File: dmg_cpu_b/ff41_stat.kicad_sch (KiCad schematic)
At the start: 134 parts

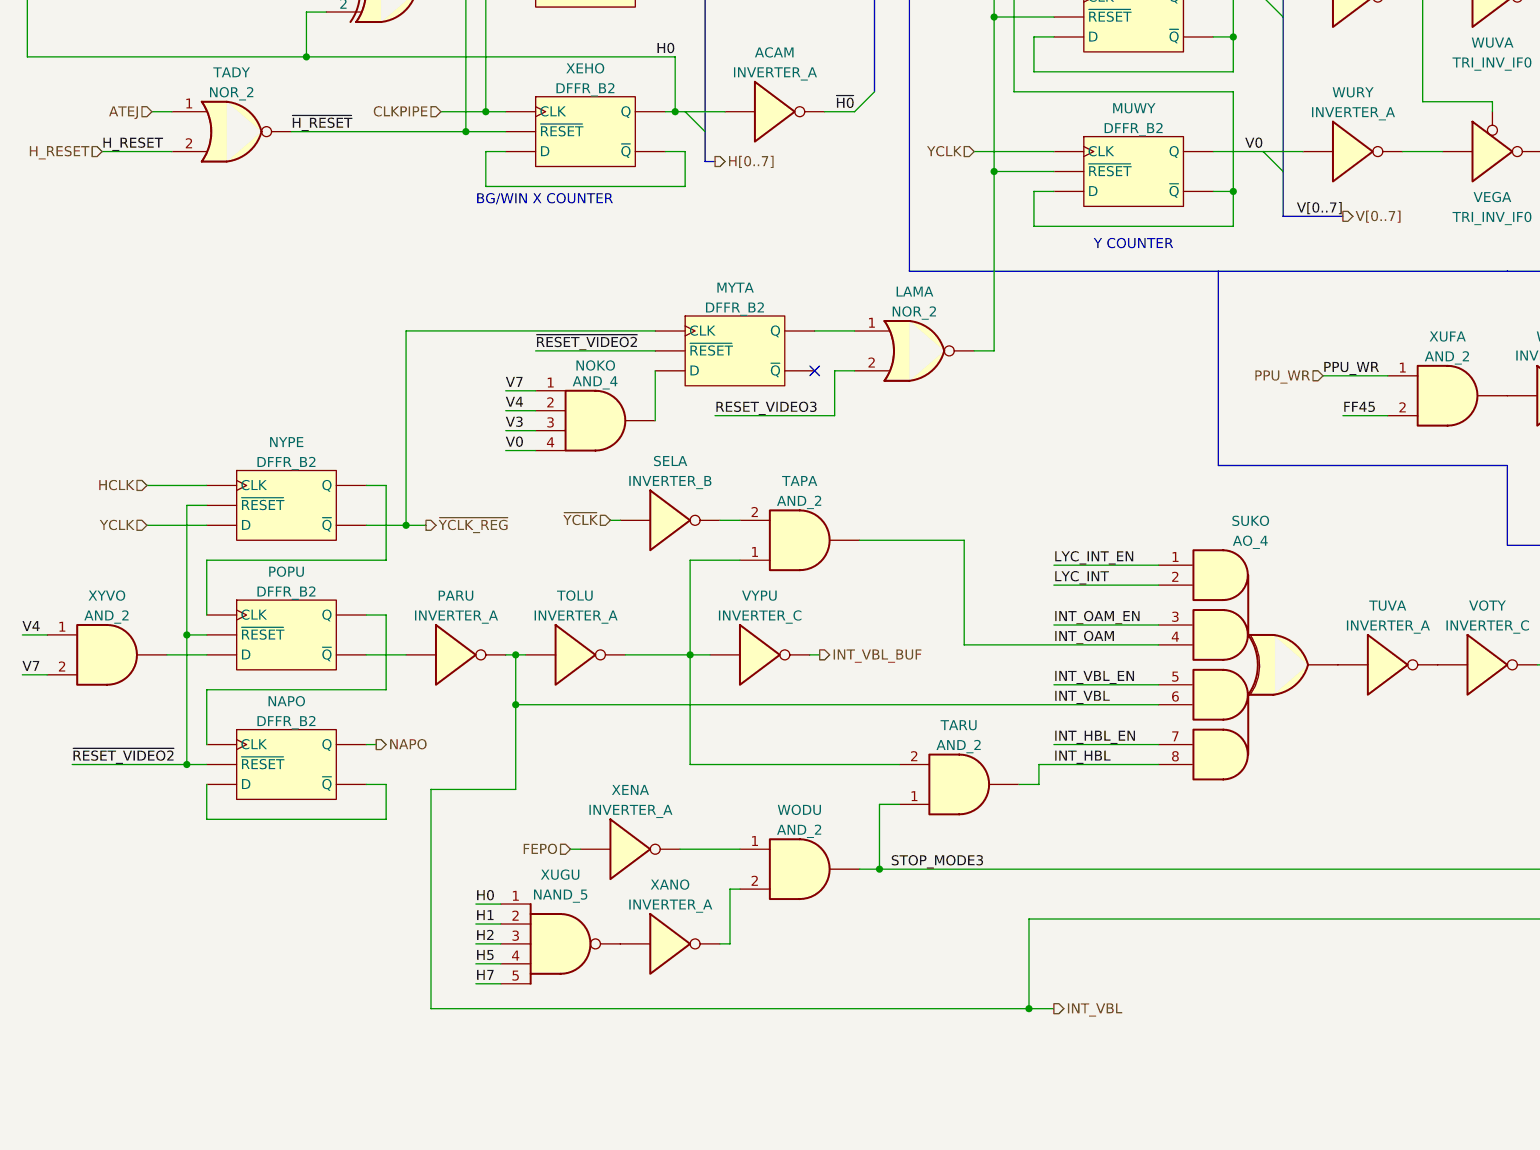
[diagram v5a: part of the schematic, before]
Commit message: sprite y comparator added
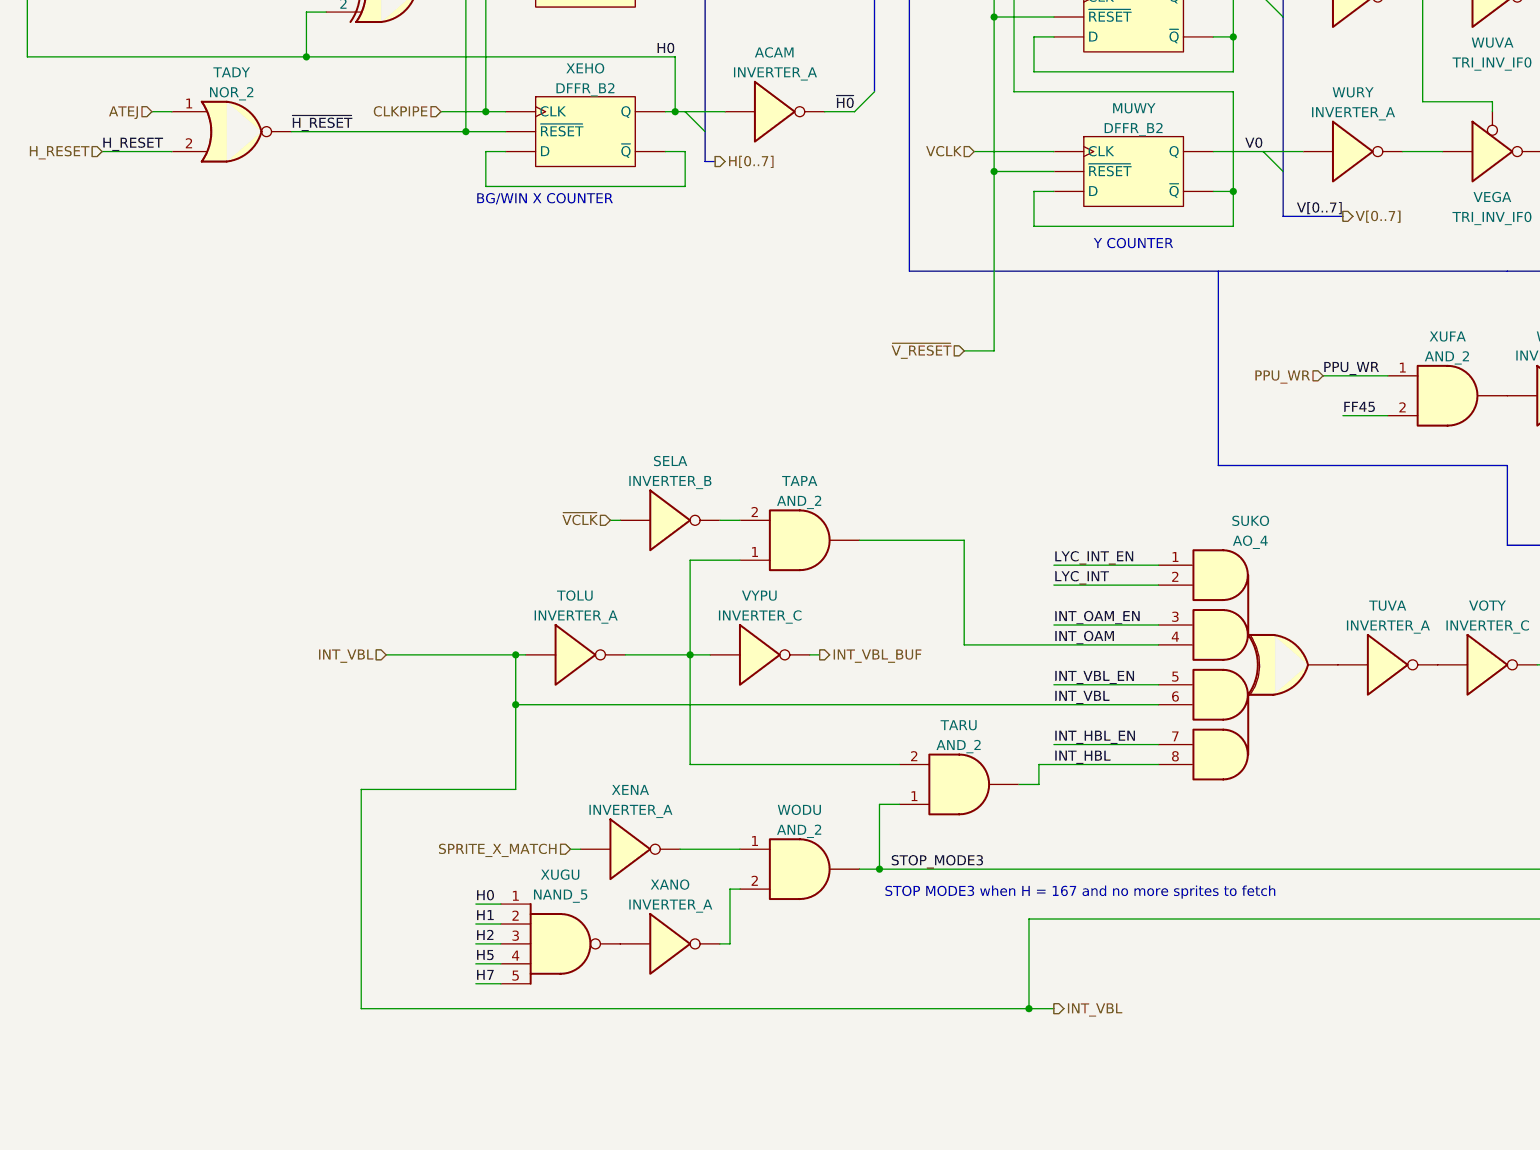
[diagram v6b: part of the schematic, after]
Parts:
- removed LAMA: NOR_2, symbol DMG_CPU_Cells:NOR_2
- removed MYTA, NAPO, NYPE, POPU: DFFR_B2, symbol DMG_CPU_Cells:DFFR_B2
- removed NOKO: AND_4, symbol DMG_CPU_Cells:AND_4
- removed PARU: INVERTER_A, symbol DMG_CPU_Cells:INVERTER_A
- removed XYVO: AND_2, symbol DMG_CPU_Cells:AND_2
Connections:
- net ~{V_RESET}: now reaches LAFO.2 (~{RESET}), LAFO.4 (~{RESET}), LEMA.2 (~{RESET}), LEMA.4 (~{RESET}), LEXA.2 (~{RESET}), LEXA.4 (~{RESET}), LOVU.2 (~{RESET}), LOVU.4 (~{RESET}), LYDO.2 (~{RESET}), LYDO.4 (~{RESET}), MATO.2 (~{RESET}), MATO.4 (~{RESET}), MUWY.2 (~{RESET}), MUWY.4 (~{RESET}), MYRO.2 (~{RESET}), MYRO.4 (~{RESET})
- net FEPO renamed SPRITE_X_MATCH
- net YCLK renamed VCLK
- net ~{YCLK} renamed ~{VCLK}
- no-connect marks 12 -> 11
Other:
- note added: "STOP MODE3 when H = 167 and no more sprites to fetch"

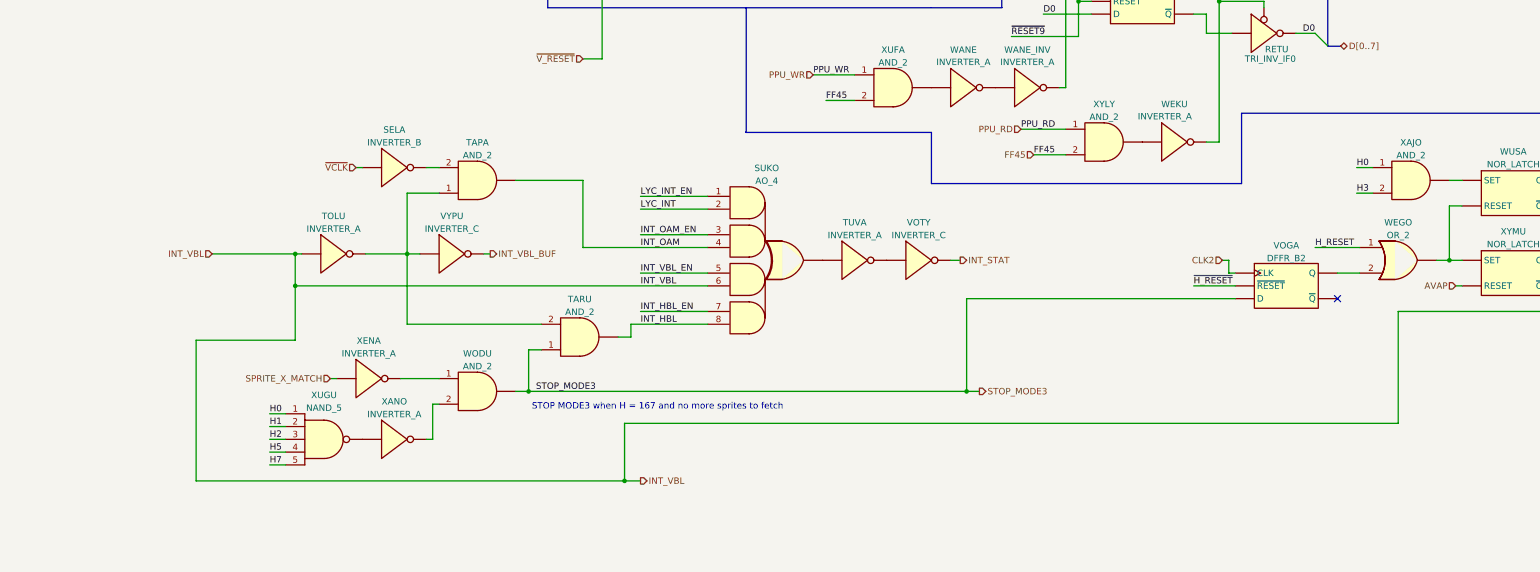
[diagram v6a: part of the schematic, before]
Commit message: more oam sheets added. Some are still work in progress.
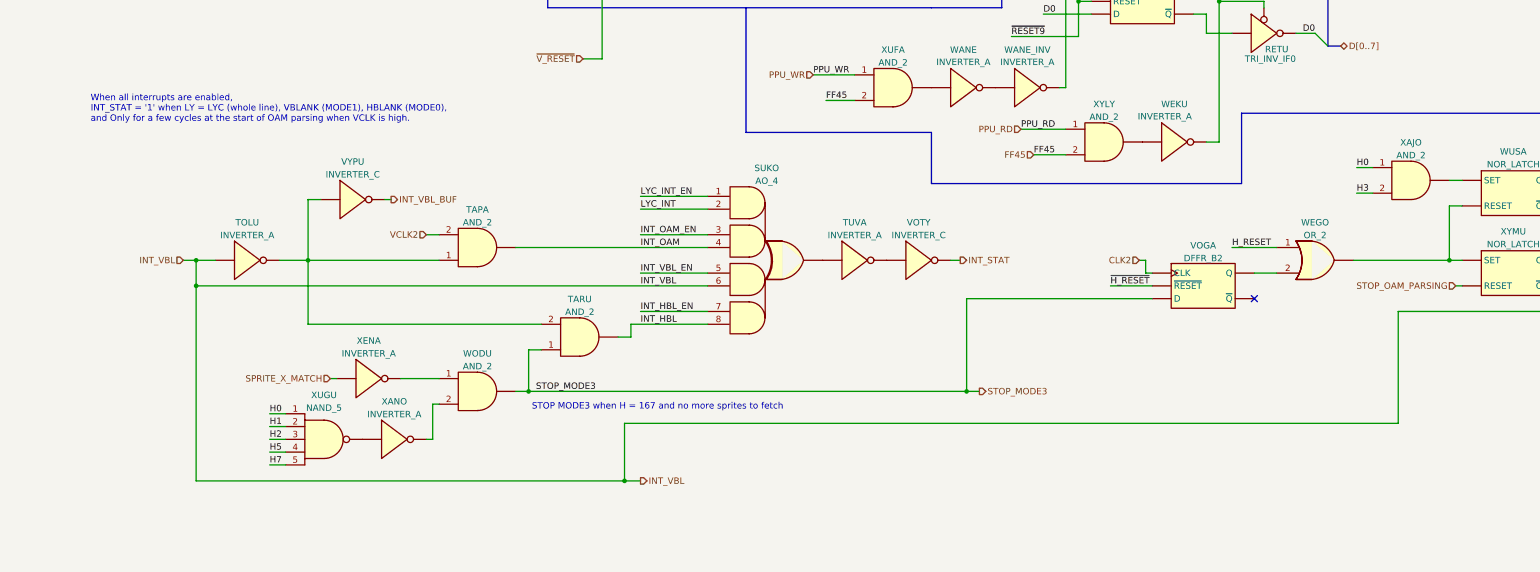
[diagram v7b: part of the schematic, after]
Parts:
- removed SELA: INVERTER_B, symbol DMG_CPU_Cells:INVERTER_B
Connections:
- net VCLK2: now reaches TAPA.2
- net AVAP renamed STOP_OAM_PARSING
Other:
- note added: "When all interrupts are enabled, INT_STAT = '1' when LY = LYC (whole line), VBLANK (MODE1), HBLANK (MODE0), and Only for a few cycles at the start of OAM parsing when VCLK is high."
- moved on the sheet: TAPA, TOLU, VOGA, VYPU, WEGO

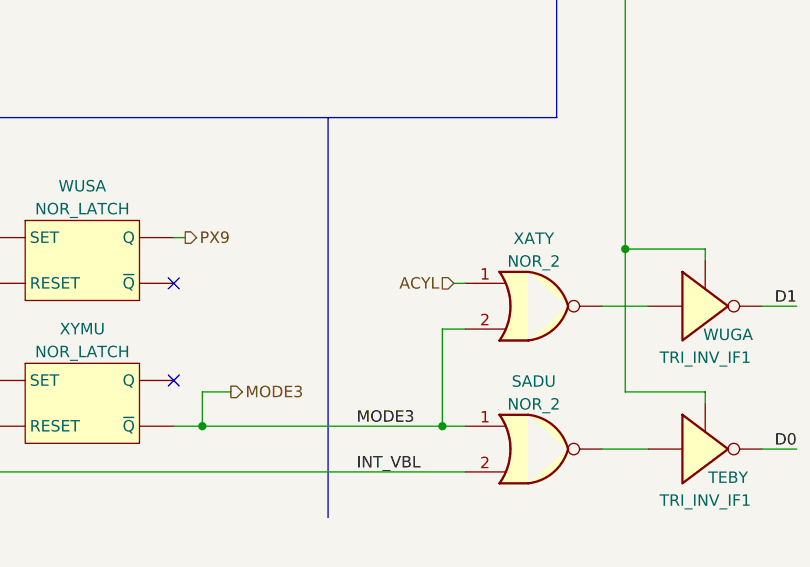
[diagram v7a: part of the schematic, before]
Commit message: More OAM sheets added.
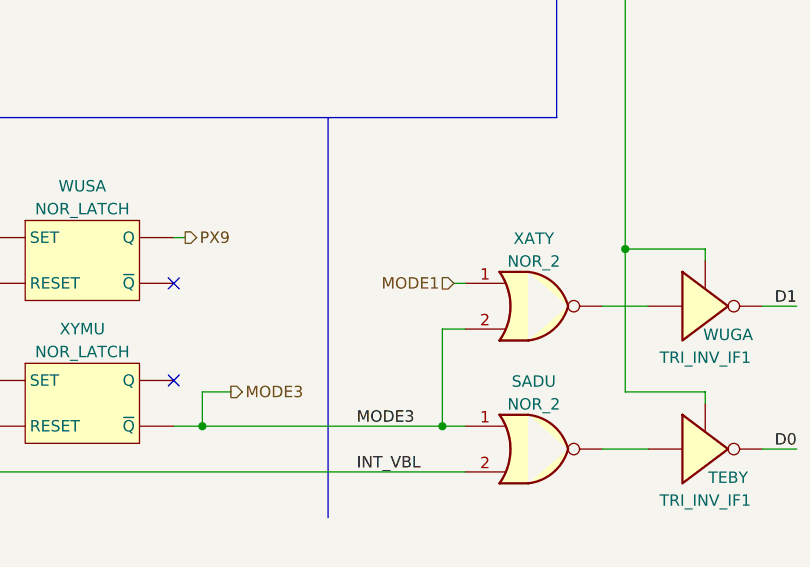
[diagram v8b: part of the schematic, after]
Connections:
- net ACYL renamed MODE1
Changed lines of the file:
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@@
     (effects (font (size 1.27 1.27)) (justify right))
   )
-  (hierarchical_label "ACYL" (shape input) (at 359.41 226.695 180)
+  (hierarchical_label "MODE1" (shape input) (at 359.41 226.695 180)
     (effects (font (size 1.27 1.27)) (justify right))
   )
